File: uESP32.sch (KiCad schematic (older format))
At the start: 26 parts, among them J1 USB_B_Micro, J2 Conn_01x14, J3 Conn_01x14, J4 Conn_01x10, J5 Conn_01x02, Q1 MMBT2222, Q2 MMBT2222, Q3 Si2323, U1 ESP32-WROOM-32, U2 CP2104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

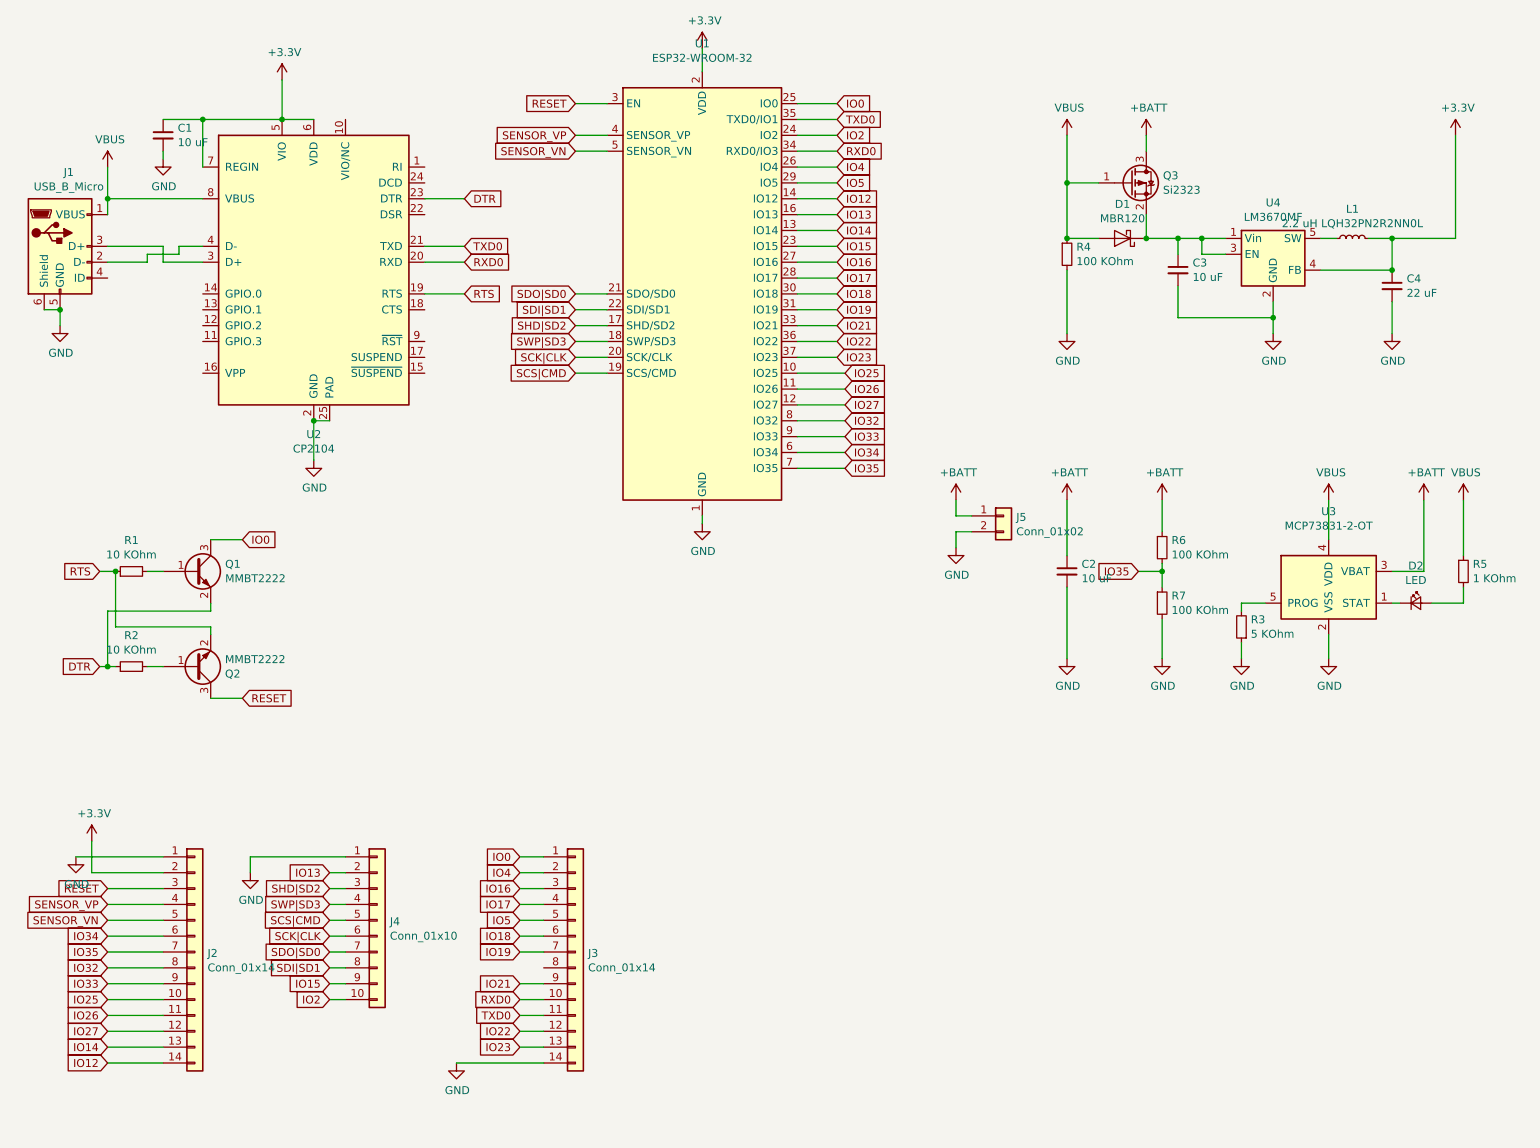
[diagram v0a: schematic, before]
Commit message: version 2 2.54 pin header
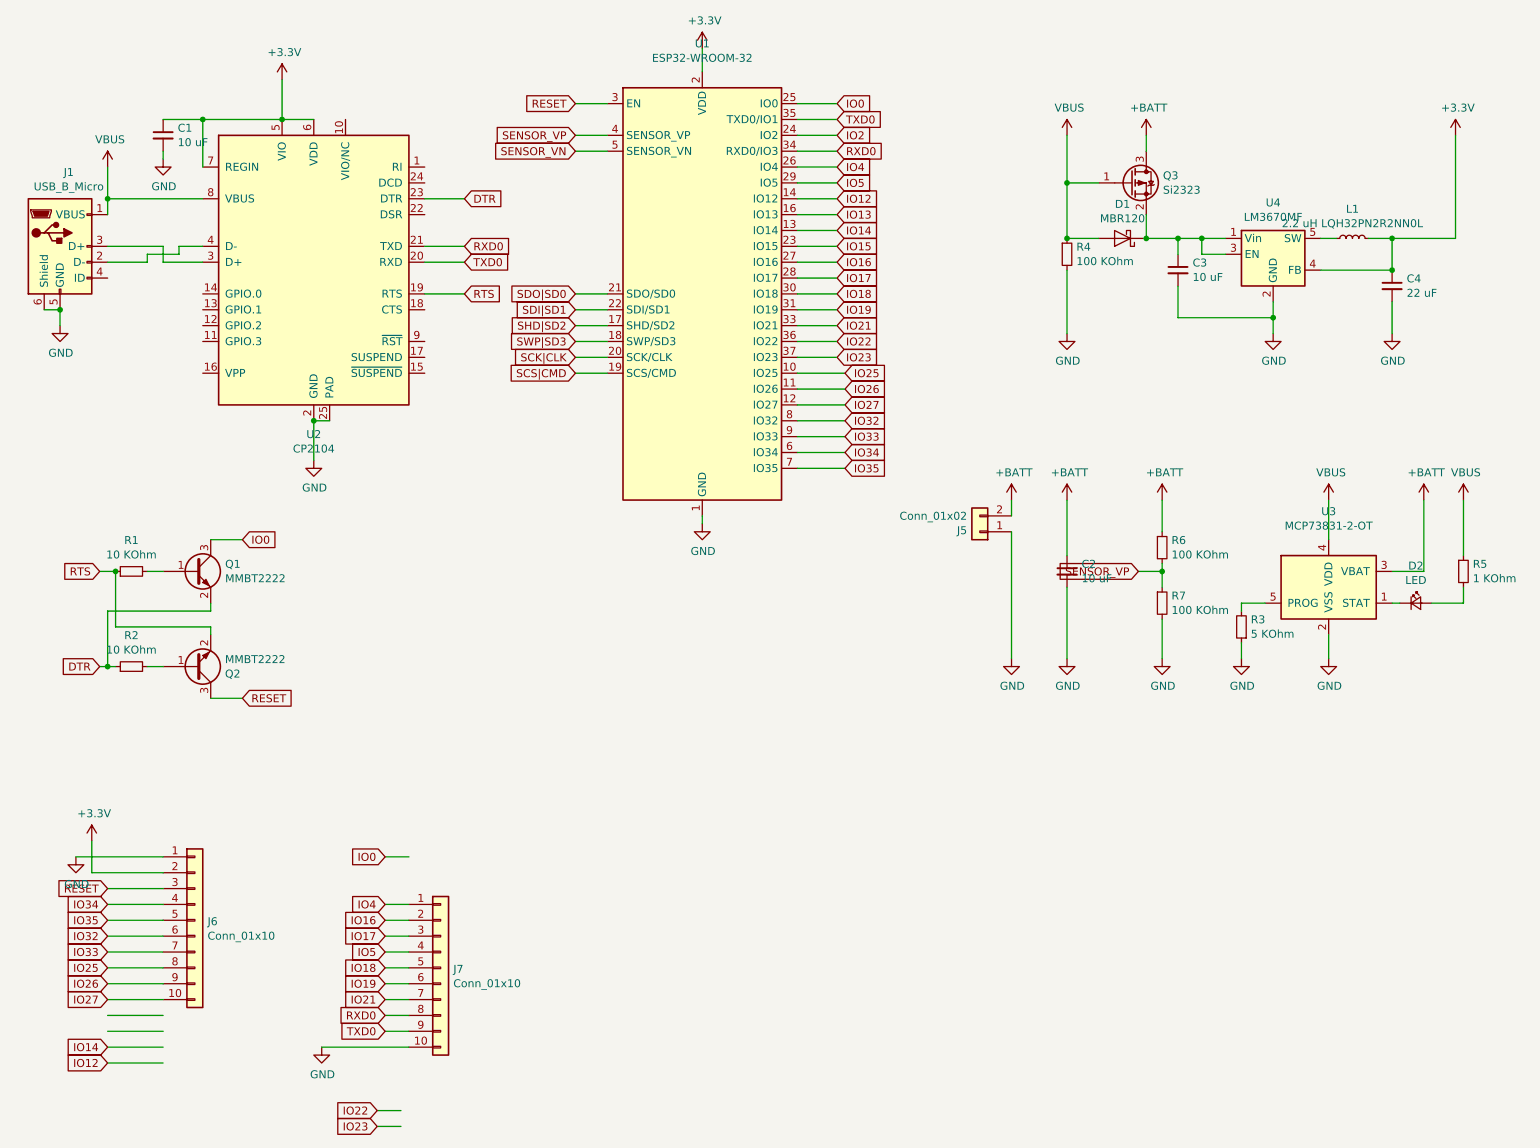
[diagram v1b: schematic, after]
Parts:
- removed J2, J3: Conn_01x14, Connector_PinHeader_1.27mm:PinHeader_1x14_P1.27mm_Vertical, symbol Connector_Generic:Conn_01x14
- removed J4: Conn_01x10, Connector_PinHeader_1.27mm:PinHeader_1x10_P1.27mm_Vertical, symbol Connector_Generic:Conn_01x10
- added J6, J7: Conn_01x10, Connector_PinHeader_2.54mm:PinHeader_1x10_P2.54mm_Vertical, symbol Connector_Generic:Conn_01x10
- D2: footprint LED_SMD:LED_0402_1005Metric -> LED_SMD:LED_1806_4516Metric
- J1: footprint Connector_USB:USB_Micro-B_Molex-105017-0001 -> Connector_USB:USB_Micro-B_Molex_47346-0001
- J5: footprint Connector_PinHeader_1.27mm:PinHeader_1x02_P1.27mm_Vertical -> Connector_JST:JST_GH_BM02B-GHS-TBT_1x02-1MP_P1.25mm_Vertical
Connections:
- wire segments 158 -> 145
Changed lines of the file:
@@
 F 0 "J1" H 955 2417 50  0000 C CNN
 F 1 "USB_B_Micro" H 955 2326 50  0000 C CNN
-F 2 "Connector_USB:USB_Micro-B_Molex-105017-0001" H 1050 1900 50  0001 C CNN
+F 2 "Connector_USB:USB_Micro-B_Molex_47346-0001" H 1050 1900 50  0001 C CNN
 F 3 "~" H 1050 1900 50  0001 C CNN
 	1    900  1950
@@
 Text GLabel 3450 1650 2    50   Input ~ 0
 DTR
+Text GLabel 3450 2050 2    50   Input ~ 0
+TXD0
 Text GLabel 3450 1950 2    50   Input ~ 0
-TXD0
-Text GLabel 3450 2050 2    50   Input ~ 0
 RXD0
 Text GLabel 3450 2250 2    50   Input ~ 0
@@
 F 0 "D2" H 9450 4435 50  0000 C CNN
 F 1 "LED" H 9450 4344 50  0000 C CNN
-F 2 "LED_SMD:LED_0402_1005Metric" V 9450 4200 50  0001 C CNN
+F 2 "LED_SMD:LED_1806_4516Metric" V 9450 4200 50  0001 C CNN
 F 3 "~" V 9450 4200 50  0001 C CNN
 	1    9450 4200
@@
 Wire Wire Line
 	5550 3350 5850 3350
-Text GLabel 7700 4000 0    50   Input ~ 0
-IO35
 Wire Wire Line
 	7700 4000 7850 4000
@@
 	9300 1900 9700 1900
 $Comp
-L Connector_Generic:Conn_01x14 J2
-U 1 1 5E6405A3
-P 1750 6400
-F 0 "J2" H 1830 6392 50  0000 L CNN
-F 1 "Conn_01x14" H 1830 6301 50  0000 L CNN
-F 2 "Connector_PinHeader_1.27mm:PinHeader_1x14_P1.27mm_Vertical" H 1750 6400 50  0001 C CNN
-F 3 "~" H 1750 6400 50  0001 C CNN
-	1    1750 6400
-	1    0    0    -1
-$EndComp
-$Comp
-L Connector_Generic:Conn_01x14 J3
-U 1 1 5E64086A
-P 4150 6400
-F 0 "J3" H 4230 6392 50  0000 L CNN
-F 1 "Conn_01x14" H 4230 6301 50  0000 L CNN
-F 2 "Connector_PinHeader_1.27mm:PinHeader_1x14_P1.27mm_Vertical" H 4150 6400 50  0001 C CNN
-F 3 "~" H 4150 6400 50  0001 C CNN
-	1    4150 6400
-	1    0    0    -1
-$EndComp
-$Comp
-L Connector_Generic:Conn_01x10 J4
-U 1 1 5E6409C8
-P 2900 6200
-F 0 "J4" H 2980 6192 50  0000 L CNN
-F 1 "Conn_01x10" H 2980 6101 50  0000 L CNN
-F 2 "Connector_PinHeader_1.27mm:PinHeader_1x10_P1.27mm_Vertical" H 2900 6200 50  0001 C CNN
-F 3 "~" H 2900 6200 50  0001 C CNN
-	1    2900 6200
-	1    0    0    -1
-$EndComp
-$Comp
 L power:GND #PWR0123
 U 1 1 5E640F6D
@@
 Wire Wire Line
 	4350 1350 4150 1350
-Text GLabel 1200 6100 0    50   Input ~ 0
-SENSOR_VP
-Text GLabel 1200 6200 0    50   Input ~ 0
-SENSOR_VN
 Wire Wire Line
 	1200 6100 1550 6100
@@
 Wire Wire Line
 	5850 3250 5550 3250
-Text GLabel 1200 6300 0    50   Input ~ 0
+Text GLabel 1200 6100 0    50   Input ~ 0
 IO34
-Text GLabel 1200 6400 0    50   Input ~ 0
+Text GLabel 1200 6200 0    50   Input ~ 0
 IO35
 Wire Wire Line
@@
 Text GLabel 5850 2950 2    50   Input ~ 0
 IO27
+Text GLabel 1200 6300 0    50   Input ~ 0
+IO32
+Text GLabel 1200 6400 0    50   Input ~ 0
+IO33
 Text GLabel 1200 6500 0    50   Input ~ 0
-IO32
+IO25
 Text GLabel 1200 6600 0    50   Input ~ 0
-IO33
+IO26
 Text GLabel 1200 6700 0    50   Input ~ 0
-IO25
-Text GLabel 1200 6800 0    50   Input ~ 0
-IO26
-Text GLabel 1200 6900 0    50   Input ~ 0
 IO27
 Text GLabel 5800 1650 2    50   Input ~ 0
@@
 	1200 7100 1550 7100
 $Comp
-L power:GND #PWR0125
-U 1 1 5E6B7301
-P 2100 5900
-F 0 "#PWR0125" H 2100 5650 50  0001 C CNN
-F 1 "GND" H 2105 5727 50  0000 C CNN
-F 2 "" H 2100 5900 50  0001 C CNN
-F 3 "" H 2100 5900 50  0001 C CNN
-	1    2100 5900
-	1    0    0    -1
-$EndComp
-Wire Wire Line
-	2700 5800 2100 5800
-Wire Wire Line
-	2100 5800 2100 5900
-$Comp
 L Connector_Generic:Conn_01x02 J5
 U 1 1 5E6BEB48
-P 6850 3650
-F 0 "J5" H 6930 3642 50  0000 L CNN
-F 1 "Conn_01x02" H 6930 3551 50  0000 L CNN
-F 2 "Connector_PinHeader_1.27mm:PinHeader_1x02_P1.27mm_Vertical" H 6850 3650 50  0001 C CNN
-F 3 "~" H 6850 3650 50  0001 C CNN
-	1    6850 3650
-	1    0    0    -1
+P 6700 3750
+F 0 "J5" H 6780 3742 50  0000 L CNN
+F 1 "Conn_01x02" H 6780 3651 50  0000 L CNN
+F 2 "Connector_JST:JST_GH_BM02B-GHS-TBT_1x02-1MP_P1.25mm_Vertical" H 6700 3750 50  0001 C CNN
+F 3 "~" H 6700 3750 50  0001 C CNN
+	1    6700 3750
+	-1   0    0    1
 $EndComp
 $Comp
 L power:GND #PWR0126
 U 1 1 5E6BEE5E
-P 6550 3850
-F 0 "#PWR0126" H 6550 3600 50  0001 C CNN
-F 1 "GND" H 6555 3677 50  0000 C CNN
-F 2 "" H 6550 3850 50  0001 C CNN
-F 3 "" H 6550 3850 50  0001 C CNN
-	1    6550 3850
+P 6900 4550
+F 0 "#PWR0126" H 6900 4300 50  0001 C CNN
+F 1 "GND" H 6905 4377 50  0000 C CNN
+F 2 "" H 6900 4550 50  0001 C CNN
+F 3 "" H 6900 4550 50  0001 C CNN
+	1    6900 4550
 	1    0    0    -1
 $EndComp
@@
 L power:+BATT #PWR0127
 U 1 1 5E6BEEDC
-P 6550 3550
-F 0 "#PWR0127" H 6550 3400 50  0001 C CNN
-F 1 "+BATT" H 6565 3723 50  0000 C CNN
-F 2 "" H 6550 3550 50  0001 C CNN
-F 3 "" H 6550 3550 50  0001 C CNN
-	1    6550 3550
-	1    0    0    -1
-$EndComp
-Wire Wire Line
-	6650 3650 6550 3650
-Wire Wire Line
-	6550 3650 6550 3550
-Wire Wire Line
-	6550 3850 6550 3750
-Wire Wire Line
-	6550 3750 6650 3750
+P 6900 3550
+F 0 "#PWR0127" H 6900 3400 50  0001 C CNN
+F 1 "+BATT" H 6915 3723 50  0000 C CNN
+F 2 "" H 6900 3550 50  0001 C CNN
+F 3 "" H 6900 3550 50  0001 C CNN
+	1    6900 3550
+	1    0    0    -1
+$EndComp
+Wire Wire Line
+	6900 3650 6900 3550
 Text GLabel 5800 1750 2    50   Input ~ 0
-IO13
-Text GLabel 2600 5900 0    50   Input ~ 0
 IO13
 Wire Wire Line
@@
 Text GLabel 4150 2350 0    50   Input ~ 0
 SDI|SD1
-Text GLabel 2600 6000 0    50   Input ~ 0
-SHD|SD2
-Text GLabel 2600 6100 0    50   Input ~ 0
-SWP|SD3
-Text GLabel 2600 6200 0    50   Input ~ 0
-SCS|CMD
-Text GLabel 2600 6300 0    50   Input ~ 0
-SCK|CLK
-Text GLabel 2600 6400 0    50   Input ~ 0
-SDO|SD0
-Text GLabel 2600 6500 0    50   Input ~ 0
-SDI|SD1
-Wire Wire Line
-	2600 5900 2700 5900
 Wire Wire Line
 	4350 2250 4150 2250
@@
 Wire Wire Line
 	4150 2750 4350 2750
-Wire Wire Line
-	2700 6000 2600 6000
-Wire Wire Line
-	2600 6100 2700 6100
-Wire Wire Line
-	2700 6200 2600 6200
-Wire Wire Line
-	2600 6300 2700 6300
-Wire Wire Line
-	2700 6400 2600 6400
-Wire Wire Line
-	2600 6500 2700 6500
 Text GLabel 5800 1250 2    50   Input ~ 0
 IO2
@@
 Wire Wire Line
 	5800 1950 5550 1950
-Text GLabel 2600 6600 0    50   Input ~ 0
-IO15
-Text GLabel 2600 6700 0    50   Input ~ 0
-IO2
-Wire Wire Line
-	2700 6600 2600 6600
-Wire Wire Line
-	2600 6700 2700 6700
-Text GLabel 3800 5800 0    50   Input ~ 0
+Text GLabel 2950 5800 0    50   Input ~ 0
 IO0
 Wire Wire Line
-	3950 5800 3800 5800
+	3100 5800 2950 5800
 Text GLabel 5800 1450 2    50   Input ~ 0
 IO4
@@
 Wire Wire Line
 	5550 2350 5800 2350
-Text GLabel 3800 5900 0    50   Input ~ 0
+Text GLabel 2950 6100 0    50   Input ~ 0
 IO4
-Text GLabel 3800 6000 0    50   Input ~ 0
+Text GLabel 2950 6200 0    50   Input ~ 0
 IO16
-Text GLabel 3800 6100 0    50   Input ~ 0
+Text GLabel 2950 6300 0    50   Input ~ 0
 IO17
-Text GLabel 3800 6200 0    50   Input ~ 0
+Text GLabel 2950 6400 0    50   Input ~ 0
 IO5
-Text GLabel 3800 6300 0    50   Input ~ 0
+Text GLabel 2950 6500 0    50   Input ~ 0
 IO18
-Text GLabel 3800 6400 0    50   Input ~ 0
+Text GLabel 2950 6600 0    50   Input ~ 0
 IO19
 Wire Wire Line
-	3800 5900 3950 5900
-Wire Wire Line
-	3950 6000 3800 6000
-Wire Wire Line
-	3800 6100 3950 6100
-Wire Wire Line
-	3950 6200 3800 6200
-Wire Wire Line
-	3800 6300 3950 6300
-Wire Wire Line
-	3950 6400 3800 6400
+	2950 6100 3100 6100
+Wire Wire Line
+	3100 6200 2950 6200
+Wire Wire Line
+	2950 6300 3100 6300
+Wire Wire Line
+	3100 6400 2950 6400
+Wire Wire Line
+	2950 6500 3100 6500
+Wire Wire Line
+	3100 6600 2950 6600
 Text GLabel 5800 2450 2    50   Input ~ 0
 IO21
-Text GLabel 3800 6600 0    50   Input ~ 0
+Text GLabel 2950 6700 0    50   Input ~ 0
 IO21
-Text GLabel 3800 6700 0    50   Input ~ 0
+Text GLabel 2950 6800 0    50   Input ~ 0
 RXD0
-Text GLabel 3800 6800 0    50   Input ~ 0
+Text GLabel 2950 6900 0    50   Input ~ 0
 TXD0
 Wire Wire Line
-	3800 6600 3950 6600
-Wire Wire Line
-	3800 6700 3950 6700
-Wire Wire Line
-	3950 6800 3800 6800
-$Comp
-L power:GND #PWR?
+	2950 6700 3100 6700
+Wire Wire Line
+	2950 6800 3100 6800
+Wire Wire Line
+	3100 6900 2950 6900
+$Comp
+L power:GND #PWR0128
 U 1 1 5E742FE0
-P 3400 7100
-F 0 "#PWR?" H 3400 6850 50  0001 C CNN
-F 1 "GND" H 3405 6927 50  0000 C CNN
-F 2 "" H 3400 7100 50  0001 C CNN
-F 3 "" H 3400 7100 50  0001 C CNN
-	1    3400 7100
-	1    0    0    -1
-$EndComp
-Wire Wire Line
-	3950 7100 3400 7100
+P 2550 7000
+F 0 "#PWR0128" H 2550 6750 50  0001 C CNN
+F 1 "GND" H 2555 6827 50  0000 C CNN
+F 2 "" H 2550 7000 50  0001 C CNN
+F 3 "" H 2550 7000 50  0001 C CNN
+	1    2550 7000
+	1    0    0    -1
+$EndComp
+Wire Wire Line
+	3100 7000 2550 7000
 Text GLabel 5800 2550 2    50   Input ~ 0
 IO22
@@
 Wire Wire Line
 	5800 2650 5550 2650
-Text GLabel 3800 6900 0    50   Input ~ 0
+Text GLabel 2900 7400 0    50   Input ~ 0
 IO22
-Text GLabel 3800 7000 0    50   Input ~ 0
+Text GLabel 2900 7500 0    50   Input ~ 0
 IO23
 Wire Wire Line
-	3800 6900 3950 6900
-Wire Wire Line
-	3950 7000 3800 7000
+	2900 7400 3050 7400
+Wire Wire Line
+	3050 7500 2900 7500
+$Comp
+L Connector_Generic:Conn_01x10 J6
+U 1 1 5E6F2241
+P 1750 6200
+F 0 "J6" H 1830 6192 50  0000 L CNN
+F 1 "Conn_01x10" H 1830 6101 50  0000 L CNN
+F 2 "Connector_PinHeader_2.54mm:PinHeader_1x10_P2.54mm_Vertical" H 1750 6200 50  0001 C CNN
+F 3 "~" H 1750 6200 50  0001 C CNN
+	1    1750 6200
+	1    0    0    -1
+$EndComp
+$Comp
+L Connector_Generic:Conn_01x10 J7
+U 1 1 5E6F22E8
+P 3300 6500
+F 0 "J7" H 3380 6492 50  0000 L CNN
+F 1 "Conn_01x10" H 3380 6401 50  0000 L CNN
+F 2 "Connector_PinHeader_2.54mm:PinHeader_1x10_P2.54mm_Vertical" H 3300 6500 50  0001 C CNN
+F 3 "~" H 3300 6500 50  0001 C CNN
+	1    3300 6500
+	1    0    0    -1
+$EndComp
+Wire Wire Line
+	6900 3750 6900 4550
+Text GLabel 7700 4000 0    50   Input ~ 0
+SENSOR_VP
 $EndSCHEMATC
